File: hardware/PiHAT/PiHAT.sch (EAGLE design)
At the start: 41 parts, among them U1 ATMEGA328P, U2 TSL2561, U3 OPA344, U4 MPL115A, U6 ADMP401, U7 SHT31-DIS, Y1 16MHZ

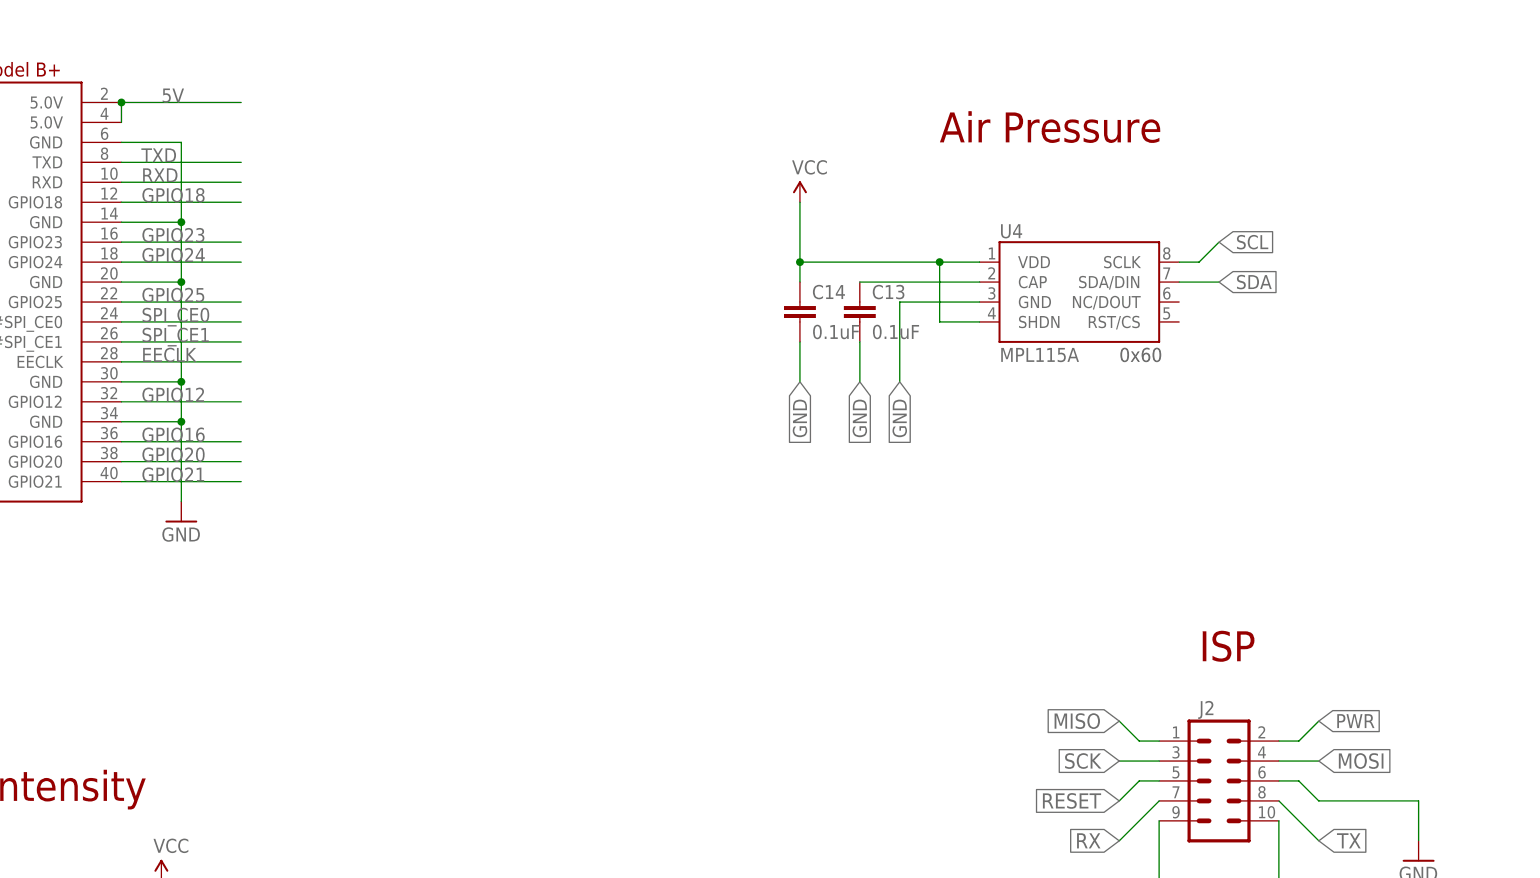
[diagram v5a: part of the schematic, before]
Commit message: Updated silkscreen
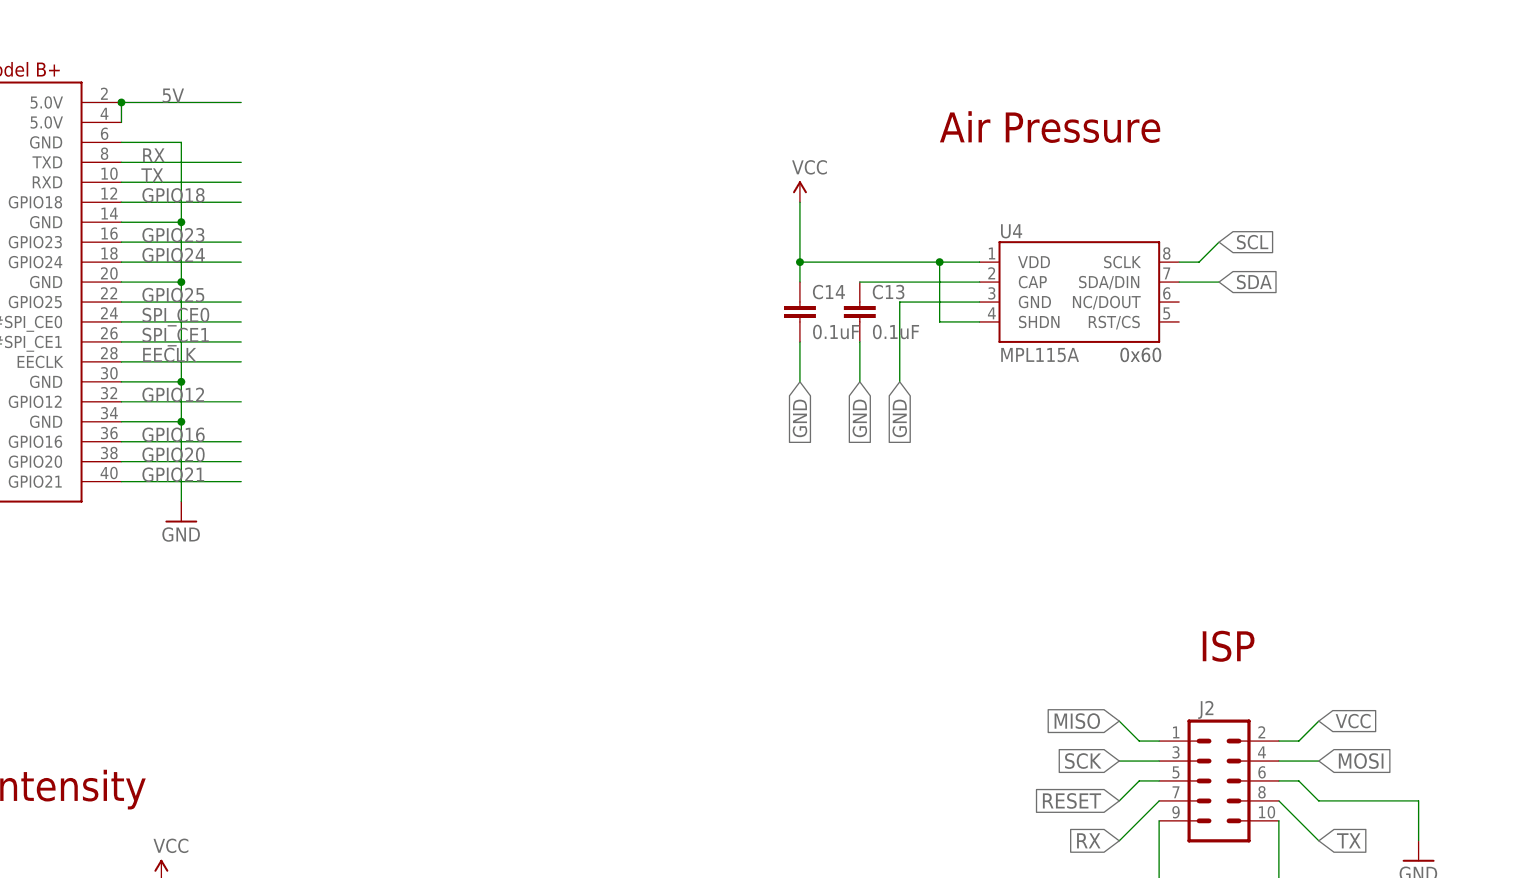
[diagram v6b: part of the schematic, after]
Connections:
- removed net PWR: J2.2
- removed net RXD: RPI1.RXD
- removed net TXD: RPI1.TXD
- net RX: now also RPI1.TXD
- net TX: now also RPI1.RXD
- net VCC: now also J2.2
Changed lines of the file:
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@@
-</segment>
-</net>
-<net name="TXD" class="0">
-<segment>
-<pinref part="RPI1" gate="G$1" pin="TXD"/>
-<wire x1="190.5" y1="124.46" x2="205.74" y2="124.46" width="0.1524" layer="91"/>
-<label x="193.04" y="124.46" size="1.778" layer="95"/>
-</segment>
-</net>
-<net name="RXD" class="0">
-<segment>
-<pinref part="RPI1" gate="G$1" pin="RXD"/>
-<wire x1="205.74" y1="121.92" x2="190.5" y2="121.92" width="0.1524" layer="91"/>
-<label x="193.04" y="121.92" size="1.778" layer="95"/>
 </segment>
 </net>
@@
 <label x="139.7" y="132.08" size="1.778" layer="95" rot="R180" xref="yes"/>
 </segment>
+<segment>
+<pinref part="J2" gate="G$1" pin="2"/>
+<wire x1="337.82" y1="50.8" x2="340.36" y2="50.8" width="0.1524" layer="91"/>
+<wire x1="340.36" y1="50.8" x2="342.9" y2="53.34" width="0.1524" layer="91"/>
+<label x="342.9" y="53.34" size="1.778" layer="95" xref="yes"/>
+</segment>
 </net>
 <net name="D5" class="0">
@@
 <wire x1="436.88" y1="106.68" x2="429.26" y2="106.68" width="0.1524" layer="91"/>
 <wire x1="429.26" y1="106.68" x2="429.26" y2="96.52" width="0.1524" layer="91"/>
-</segment>
-</net>
-<net name="PWR" class="0">
-<segment>
-<pinref part="J2" gate="G$1" pin="2"/>
-<wire x1="337.82" y1="50.8" x2="340.36" y2="50.8" width="0.1524" layer="91"/>
-<wire x1="340.36" y1="50.8" x2="342.9" y2="53.34" width="0.1524" layer="91"/>
-<label x="342.9" y="53.34" size="1.778" layer="95" xref="yes"/>
 </segment>
 </net>
@@
 <label x="492.76" y="109.22" size="1.778" layer="95" xref="yes"/>
 </segment>
+<segment>
+<pinref part="RPI1" gate="G$1" pin="TXD"/>
+<wire x1="190.5" y1="124.46" x2="205.74" y2="124.46" width="0.1524" layer="91"/>
+<label x="193.04" y="124.46" size="1.778" layer="95"/>
+</segment>
 </net>
 <net name="TX" class="0">
@@
 <label x="492.76" y="106.68" size="1.778" layer="95" xref="yes"/>
 </segment>
-</net>
+<segment>
+<pinref part="RPI1" gate="G$1" pin="RXD"/>
+<wire x1="205.74" y1="121.92" x2="190.5" y2="121.92" width="0.1524" layer="91"/>
+<label x="193.04" y="121.92" size="1.778" layer="95"/>
+</segment>
+</net>

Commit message: Adjusted schematic
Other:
- note added: "PiAQ HAT"
- note removed: "Pi HAT"
- moved on the sheet: C12, C13, C14, C15, C3, C4, C5, IAQ-CORE, J2, LED2, R13, R4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

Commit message: adding bom values
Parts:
- U4: DIGIKEY# (none) -> MPL115A2-ND
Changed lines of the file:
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@@
 <part name="SUPPLY11" library="SparkFun-Aesthetics" deviceset="VCC" device=""/>
 <part name="J2" library="SparkFun-Connectors" deviceset="M05X2" device="PTH"/>
-<part name="U4" library="SparkFun-Sensors" deviceset="MPL115A" device=""/>
+<part name="U4" library="SparkFun-Sensors" deviceset="MPL115A" device="">
+<attribute name="DIGIKEY#" value="MPL115A2-ND"/>
+</part>
 <part name="C13" library="SparkFun-Passives" deviceset="CAP" device="0805" value="0.1uF"/>
 <part name="C14" library="SparkFun-Passives" deviceset="CAP" device="0805" value="0.1uF"/>
@@
 <instance part="SUPPLY11" gate="G$1" x="426.72" y="132.08"/>
 <instance part="J2" gate="G$1" x="187.96" y="-10.16"/>
-<instance part="U4" gate="G$1" x="325.12" y="109.22"/>
+<instance part="U4" gate="G$1" x="325.12" y="109.22">
+<attribute name="DIGIKEY#" x="325.12" y="109.22" size="1.778" layer="96" display="off"/>
+</instance>
 <instance part="C13" gate="G$1" x="297.18" y="104.14"/>
 <instance part="C14" gate="G$1" x="289.56" y="104.14"/>
